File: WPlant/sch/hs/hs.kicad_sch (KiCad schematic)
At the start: 5 parts, among them J1 Conn_01x03_Pin, U1 SN74LVC1G14DBV

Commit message: Route of WP project done
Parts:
- J1: footprint local:PinHeader_3 -> Connector_PinHeader_2.00mm:PinHeader_1x03_P2.00mm_Vertical
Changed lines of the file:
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@@
 			)
 		)
-		(property "Footprint" "local:PinHeader_3"
+		(property "Footprint" "Connector_PinHeader_2.00mm:PinHeader_1x03_P2.00mm_Vertical"
 			(at 184.15 97.79 0)
 			(effects

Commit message: Updated *.pdf of schematics
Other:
- title: (none) -> Humidity Sensor
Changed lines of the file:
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@@
 	(generator_version "8.0")
 	(paper "A4")
+	(title_block
+		(title "Humidity Sensor")
+	)
 	(junction
 		(at 107.95 97.79)

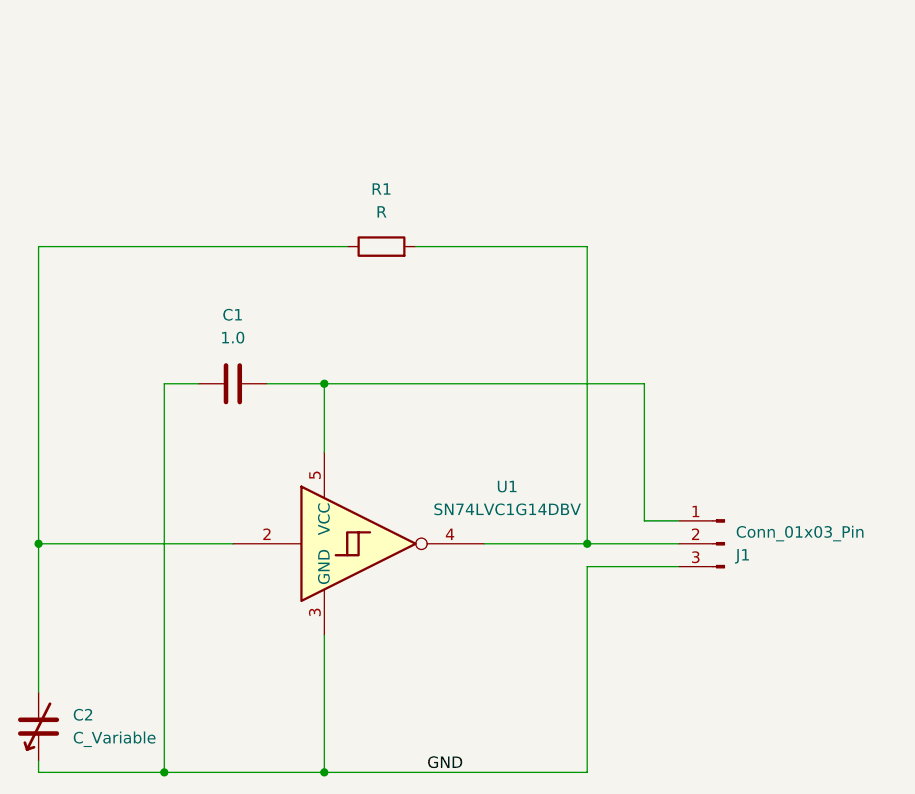
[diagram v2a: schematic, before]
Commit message: Update WP Sch (sheets titles, replaced wires by bus, update components values)
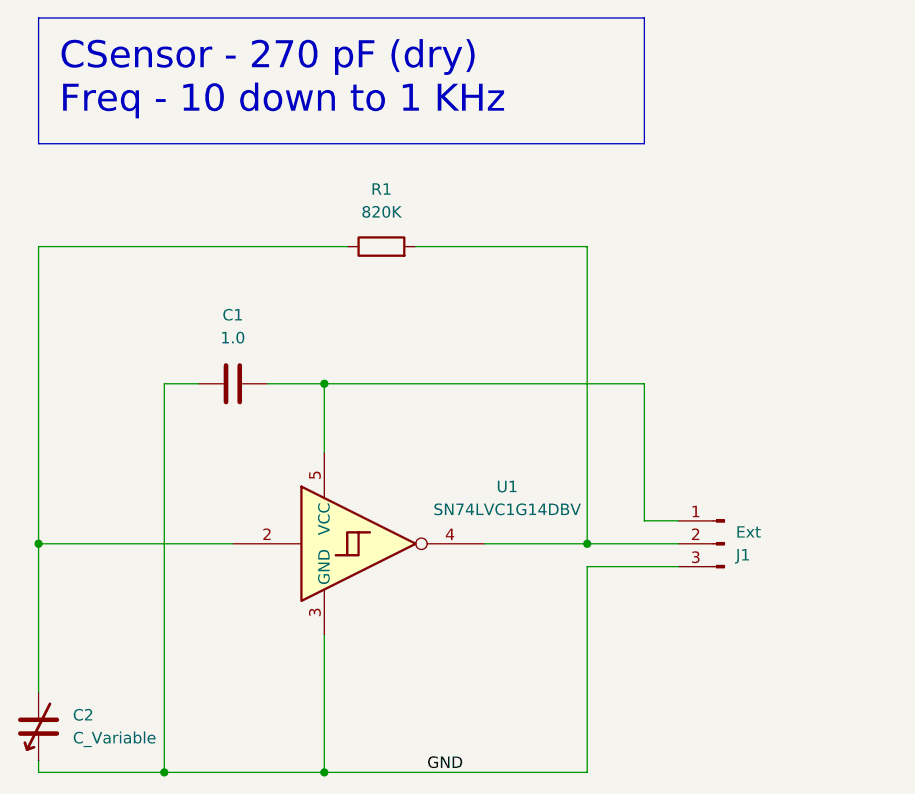
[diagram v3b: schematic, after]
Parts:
- J1: value Conn_01x03_Pin -> Ext; footprint Connector_PinHeader_2.00mm:PinHeader_1x03_P2.00mm_Vertical -> local:con3smd
- R1: value R -> 820K
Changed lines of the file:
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@@
+		)
+	)
+	(text_box "CSensor - 270 pF (dry)\nFreq - 10 down to 1 KHz"
+		(exclude_from_sim no)
+		(at 107.95 39.37 0)
+		(size 67.31 13.97)
+		(stroke
+			(width 0)
+			(type default)
+		)
+		(fill
+			(type none)
+		)
+		(effects
+			(font
+				(size 3 3)
+			)
+			(justify left top)
 		)
 	)
@@
 			)
 		)
-		(property "Value" "Conn_01x03_Pin"
+		(property "Value" "Ext"
 			(at 185.42 96.5201 0)
 			(effects
@@
 			)
 		)
-		(property "Footprint" "Connector_PinHeader_2.00mm:PinHeader_1x03_P2.00mm_Vertical"
+		(property "Footprint" "local:con3smd"
 			(at 184.15 97.79 0)
 			(effects
@@
 			)
 		)
-		(property "Value" "R"
+		(property "Value" "820K"
 			(at 146.05 60.96 90)
 			(effects

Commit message: Updated PCBs sent to JLPCB
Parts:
- C1: LCSC Part (none) -> C15849
- R1: LCSC Part (none) -> C141684
- U1: LCSC Part (none) -> C7835
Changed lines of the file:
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@@
+			)
+		)
+		(property "LCSC Part" "C7835"
+			(at 144.78 97.79 0)
+			(effects
+				(font
+					(size 1.27 1.27)
+				)
+				(hide yes)
 			)
 		)
@@
 			)
 		)
+		(property "LCSC Part" "C141684"
+			(at 146.05 64.77 0)
+			(effects
+				(font
+					(size 1.27 1.27)
+				)
+				(hide yes)
+			)
+		)
 		(pin "1"
 		)
@@
 			(at 129.54 80.01 0)
 			(effects
+				(font
+					(size 1.27 1.27)
+				)
+				(hide yes)
+			)
+		)
+		(property "LCSC Part" "C15849"
+			(at 129.54 80.01 0)
+			(effects
